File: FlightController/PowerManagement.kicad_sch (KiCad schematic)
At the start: 31 parts, among them J1 USB_C_Receptacle_USB2.0_16P, U1 AP2112K-3.3, U2 USBLC6-2SC6, U6 TPS62933, U7 TPS2115ADRBR

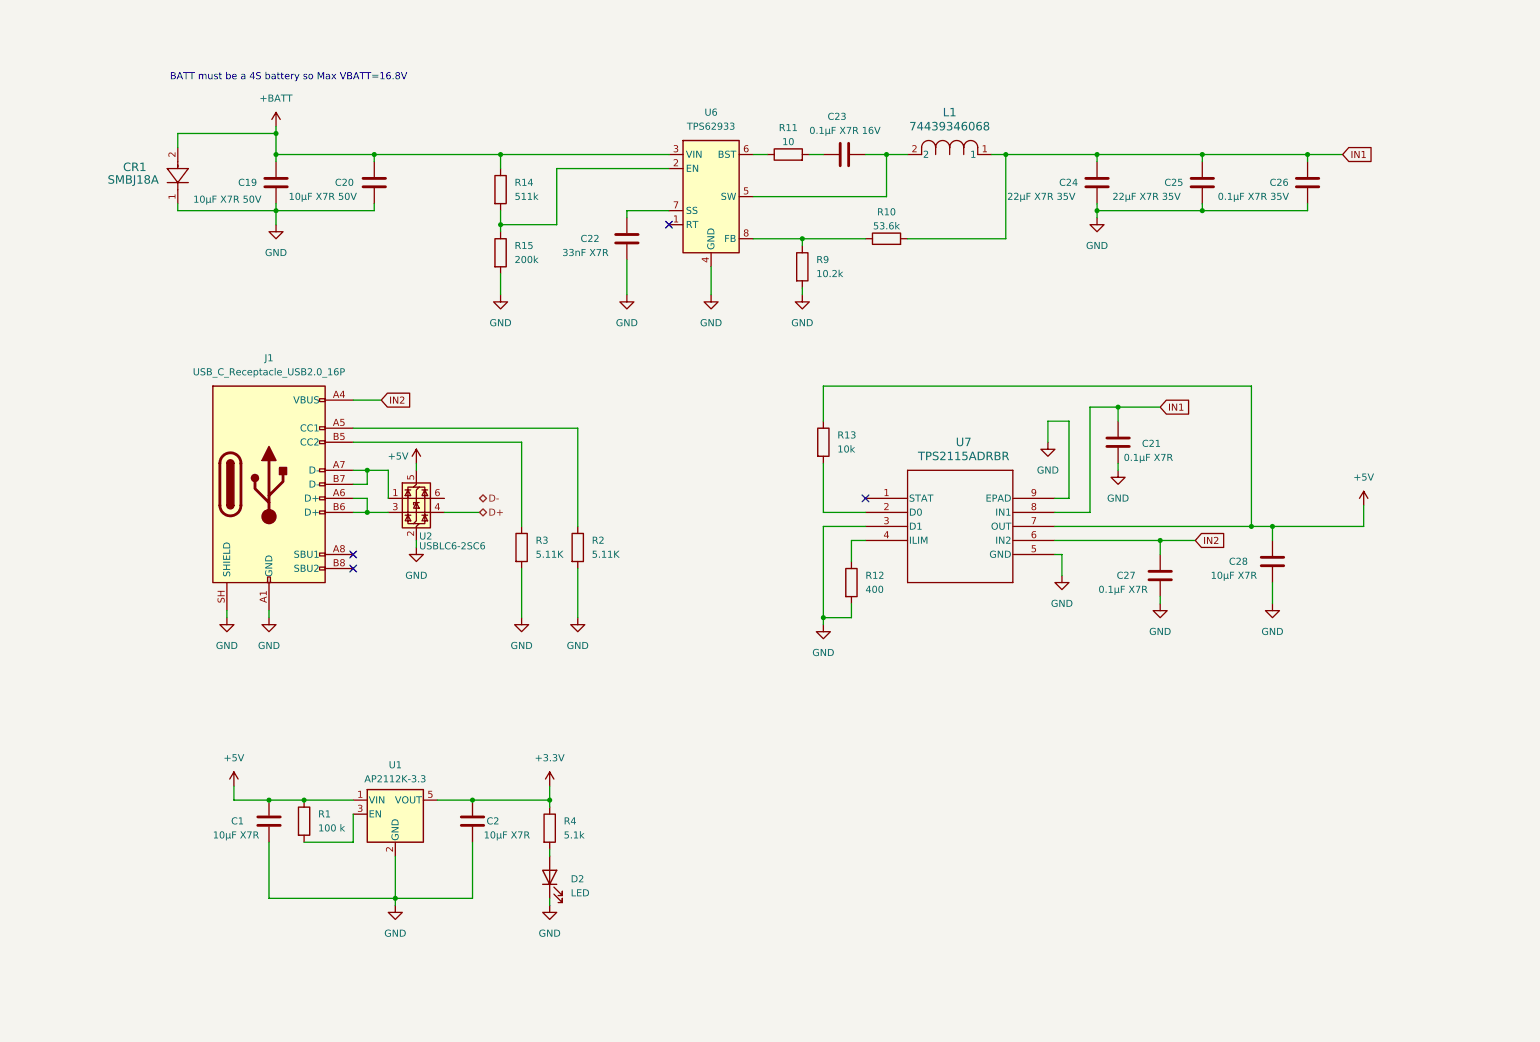
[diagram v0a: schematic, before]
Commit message: Added Part numbers and Buck in PCB
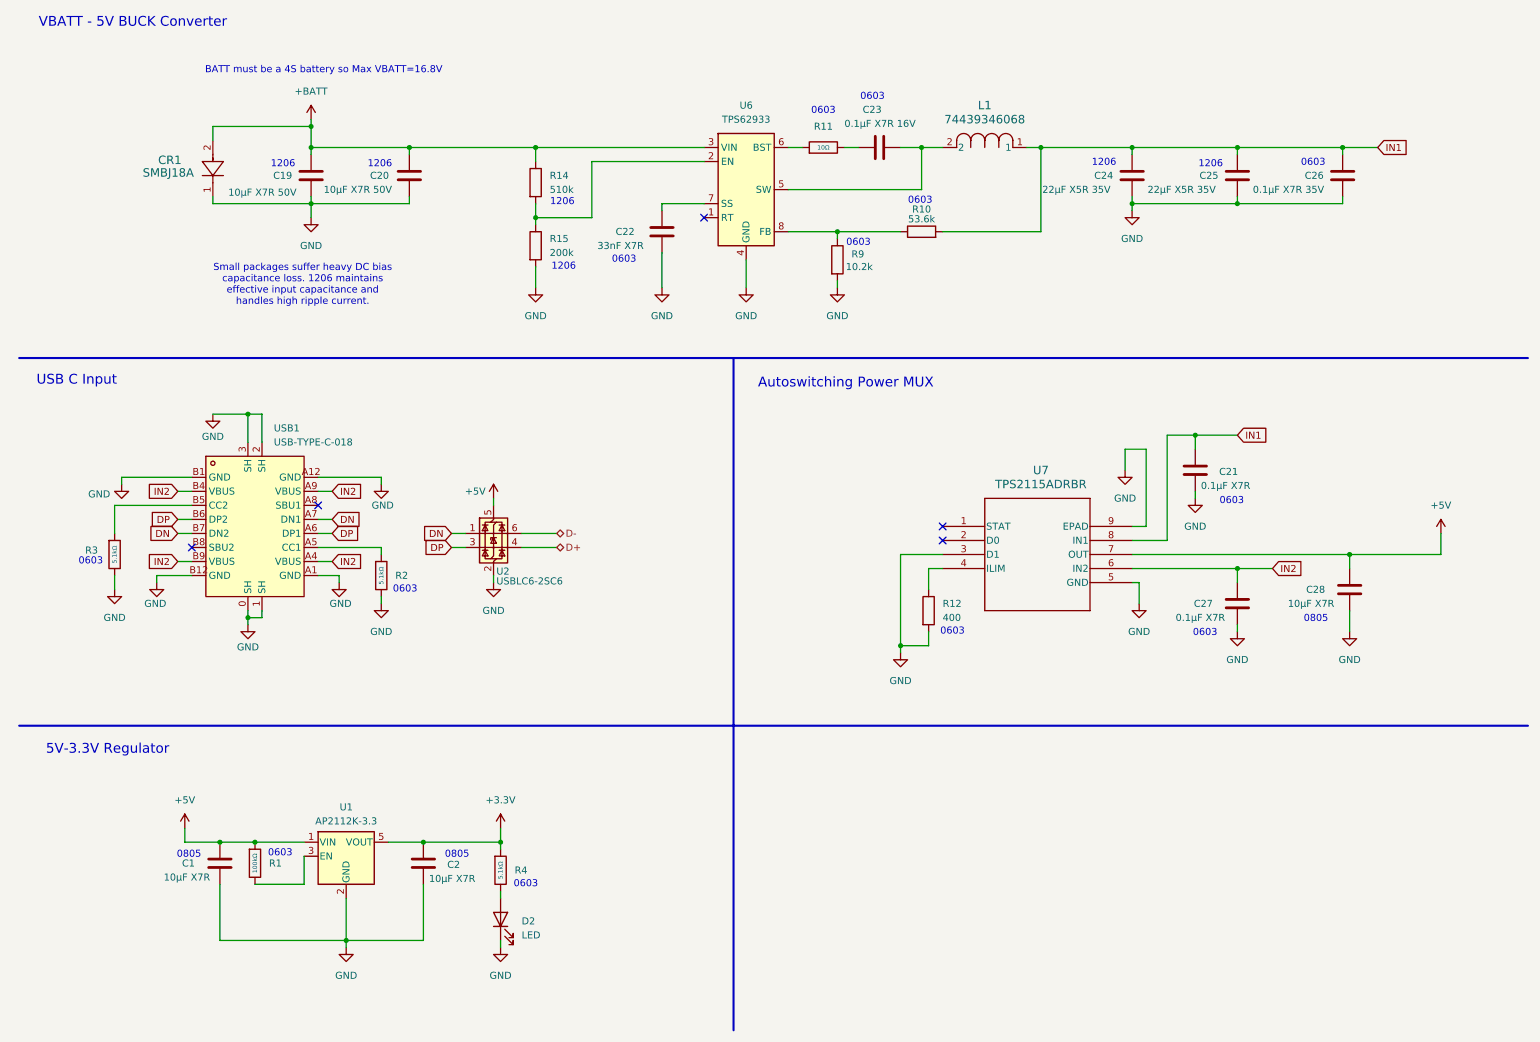
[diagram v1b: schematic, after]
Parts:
- removed J1: USB_C_Receptacle_USB2.0_16P, Connector_USB:USB_C_Receptacle_G-Switch_GT-USB-7010ASV, symbol Connector:USB_C_Receptacle_USB2.0_16P
- removed R1: 100 k, Resistor_SMD:R_1206_3216Metric_Pad1.30x1.75mm_HandSolder, symbol Device:R
- removed R11: 10, Resistor_SMD:R_1206_3216Metric_Pad1.30x1.75mm_HandSolder, symbol Device:R
- removed R13: 10k, Resistor_SMD:R_1206_3216Metric_Pad1.30x1.75mm_HandSolder, symbol Device:R
- removed R2, R3: 5.11K, Resistor_SMD:R_1206_3216Metric_Pad1.30x1.75mm_HandSolder, symbol Device:R
- removed R4: 5.1k, Resistor_SMD:R_1206_3216Metric_Pad1.30x1.75mm_HandSolder, symbol Device:R
- added R1: 100kΩ, PCM_JLCPCB:R_0603, symbol PCM_JLCPCB-Resistors:0603,100kΩ
- added R11: 10Ω, PCM_JLCPCB:R_0603, symbol PCM_JLCPCB-Resistors:0603,10Ω
- added R2, R3, R4: 5.1kΩ, PCM_JLCPCB:R_0603, symbol PCM_JLCPCB-Resistors:0603,5.1kΩ
- added USB1: USB-TYPE-C-018, USB-TYPE-C-018:USB-C_SMD-TYPE-C-31-M-12, symbol USB-TYPE-C-018:USB-TYPE-C-018
- C1, C2, C28: footprint Capacitor_SMD:C_1206_3216Metric_Pad1.33x1.80mm_HandSolder -> Capacitor_SMD:C_0805_2012Metric_Pad1.18x1.45mm_HandSolder; LCSC (none) -> C326595
- C19, C20: LCSC (none) -> C89632
- C21, C23, C27: footprint Capacitor_SMD:C_1206_3216Metric_Pad1.33x1.80mm_HandSolder -> Capacitor_SMD:C_0603_1608Metric_Pad1.08x0.95mm_HandSolder; LCSC (none) -> C1590
- C22: footprint Capacitor_SMD:C_1206_3216Metric_Pad1.33x1.80mm_HandSolder -> Capacitor_SMD:C_0603_1608Metric_Pad1.08x0.95mm_HandSolder; LCSC (none) -> C1614
- C24, C25: value 22μF X7R 35V -> 22μF X5R 35V; LCSC (none) -> C342620
- C26: footprint Capacitor_SMD:C_1206_3216Metric_Pad1.33x1.80mm_HandSolder -> Capacitor_SMD:C_0603_1608Metric_Pad1.08x0.95mm_HandSolder; LCSC (none) -> C385964
- CR1: LCSC (none) -> C10212
- D2: footprint LED_SMD:LED_1206_3216Metric_Pad1.42x1.75mm_HandSolder -> LED_SMD:LED_0603_1608Metric; LCSC (none) -> C2286
- L1: LCSC (none) -> C2041388
- R10: footprint Resistor_SMD:R_1206_3216Metric_Pad1.30x1.75mm_HandSolder -> Resistor_SMD:R_0603_1608Metric_Pad0.98x0.95mm_HandSolder; LCSC (none) -> C23074
- R12: footprint Resistor_SMD:R_1206_3216Metric_Pad1.30x1.75mm_HandSolder -> Resistor_SMD:R_0603_1608Metric_Pad0.98x0.95mm_HandSolder; LCSC (none) -> C5841024
- R14: value 511k -> 510k; LCSC (none) -> C2774961
- R15: LCSC (none) -> C5720887
- R9: footprint Resistor_SMD:R_1206_3216Metric_Pad1.30x1.75mm_HandSolder -> Resistor_SMD:R_0603_1608Metric_Pad0.98x0.95mm_HandSolder; LCSC (none) -> C22772
- U1: LCSC (none) -> C23380830
- U2: LCSC (none) -> C7519
- U6: LCSC (none) -> C3200405
- U7: LCSC (none) -> C140321
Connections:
- net +3.3V: now also R4.1
- net +5V: now also R1.1
- net D-: now also U2.6 (I/O1)
- net GND: now also R2.2, R3.2, USB1.0 (SH), USB1.1 (SH), USB1.2 (SH), USB1.3 (SH), USB1.A1 (GND), USB1.A12 (GND), USB1.B1 (GND), USB1.B12 (GND)
- net IN2: now also USB1.A4 (VBUS), USB1.A9 (VBUS), USB1.B4 (VBUS), USB1.B9 (VBUS)
- net at D2.2 (A): now also R4.2
- net at C23.2: now also R11.2
- net DP: now reaches U2.3 (I/O2)
- net DP: now also USB1.A6 (DP1), USB1.B6 (DP2)
- net DN: now reaches U2.1 (I/O1)
- net DN: now also USB1.A7 (DN1), USB1.B7 (DN2)
- net at U1.3 (EN): now also R1.2
- net at U6.6 (BST): now also R11.1
- new net: R3.1, USB1.B5 (CC2)
- new net: R2.1, USB1.A5 (CC1)
- no-connect marks 4 -> 5
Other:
- note added: "0603"
- note added: "0805"
- note added: "1206"
- note added: "5V-3.3V Regulator"
- note added: "Autoswitching Power MUX"
- note added: "Small packages suffer heavy DC bias capacitance loss. 1206 maintains effective input capacitance and handles high ripple current."
- note added: "USB C Input"
- note added: "VBATT - 5V BUCK Converter"
- moved on the sheet: C1, C19, C2, C20, C21, C22, C23, C24, C25, C26, C27, C28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
